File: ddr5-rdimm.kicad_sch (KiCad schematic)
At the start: 20 parts, among them J2 Bus_DDR5_DDR504111002KQ, Q10 BSS138PW, Q11 BSS138PW, Q9 BSS138PW, SW3 SW_KMR211NGLFS_SMD

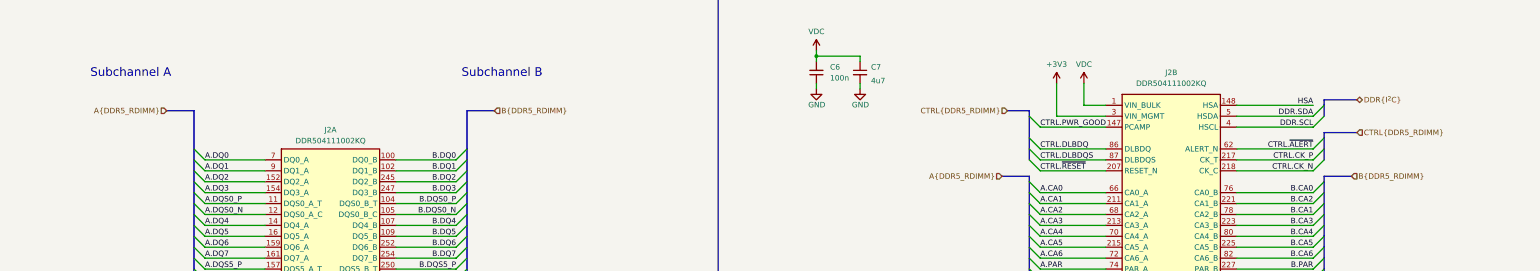
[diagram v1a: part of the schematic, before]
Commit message: [#68016] Improve bus entry marking
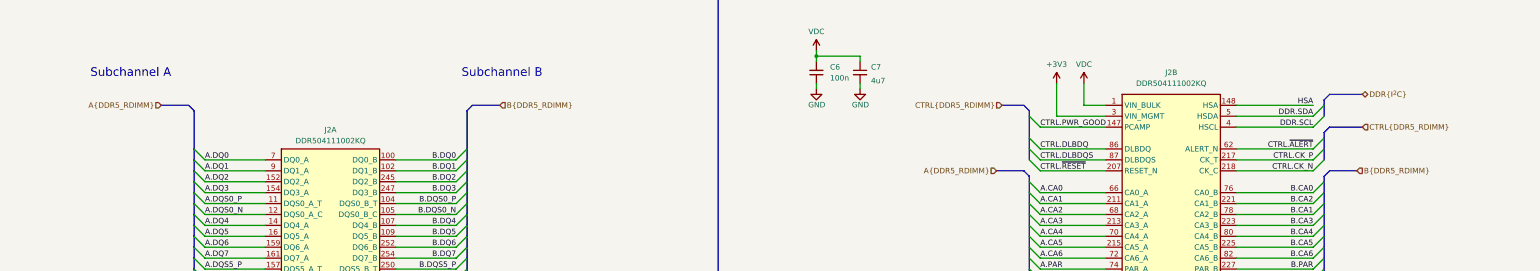
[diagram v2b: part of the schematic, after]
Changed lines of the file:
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@@
     (stroke (width 0) (type default))
   )
-  (bus (pts (xy 257.81 52.07) (xy 262.89 52.07))
+  (bus (pts (xy 256.54 50.8) (xy 261.62 50.8))
     (stroke (width 0) (type default))
   )
@@
     (stroke (width 0) (type default))
   )
+  (bus (pts (xy 262.89 67.31) (xy 261.62 66.04))
+    (stroke (width 0) (type default))
+  )
   (wire (pts (xy 71.12 76.2) (xy 85.09 76.2))
     (stroke (width 0) (type default))
@@
     (stroke (width 0) (type default))
   )
-  (bus (pts (xy 138.43 52.07) (xy 132.08 52.07))
+  (bus (pts (xy 139.7 50.8) (xy 133.35 50.8))
     (stroke (width 0) (type default))
   )
@@
     (stroke (width 0) (type default))
   )
+  (bus (pts (xy 332.74 66.04) (xy 331.47 67.31))
+    (stroke (width 0) (type default))
+  )
   (wire (pts (xy 115.57 114.3) (xy 129.54 114.3))
     (stroke (width 0) (type default))
@@
     (stroke (width 0) (type default))
   )
-  (bus (pts (xy 331.47 49.53) (xy 339.09 49.53))
+  (bus (pts (xy 332.74 48.26) (xy 340.36 48.26))
     (stroke (width 0) (type default))
   )
@@
     (stroke (width 0) (type default))
   )
+  (bus (pts (xy 67.31 50.8) (xy 68.58 52.07))
+    (stroke (width 0) (type default))
+  )
   (wire (pts (xy 71.12 147.32) (xy 85.09 147.32))
     (stroke (width 0) (type default))
@@
     (stroke (width 0) (type default))
   )
-  (bus (pts (xy 331.47 67.31) (xy 337.82 67.31))
+  (bus (pts (xy 332.74 66.04) (xy 339.09 66.04))
     (stroke (width 0) (type default))
   )
@@
     (stroke (width 0) (type default))
   )
-  (bus (pts (xy 331.47 57.15) (xy 339.09 57.15))
+  (bus (pts (xy 332.74 55.88) (xy 340.36 55.88))
     (stroke (width 0) (type default))
   )
@@
     (stroke (width 0) (type default))
   )
-  (bus (pts (xy 62.23 52.07) (xy 68.58 52.07))
+  (bus (pts (xy 60.96 50.8) (xy 67.31 50.8))
     (stroke (width 0) (type default))
   )
@@
     (stroke (width 0) (type default))
   )
+  (bus (pts (xy 262.89 52.07) (xy 261.62 50.8))
+    (stroke (width 0) (type default))
+  )
   (wire (pts (xy 313.69 114.3) (xy 313.69 111.76))
     (stroke (width 0) (type default))
@@
     (stroke (width 0) (type default))
   )
-  (bus (pts (xy 256.54 67.31) (xy 262.89 67.31))
+  (bus (pts (xy 255.27 66.04) (xy 261.62 66.04))
     (stroke (width 0) (type default))
   )
@@
     (stroke (width 0) (type default))
   )
+  (bus (pts (xy 132.08 52.07) (xy 133.35 50.8))
+    (stroke (width 0) (type default))
+  )
   (wire (pts (xy 115.57 152.4) (xy 129.54 152.4))
     (stroke (width 0) (type default))
@@
     (stroke (width 0) (type default))
   )
+  (bus (pts (xy 332.74 55.88) (xy 331.47 57.15))
+    (stroke (width 0) (type default))
+  )
   (wire (pts (xy 347.98 166.37) (xy 347.98 168.91))
     (stroke (width 0) (type default))
@@
     (stroke (width 0) (type default))
   )
+  (bus (pts (xy 332.74 48.26) (xy 331.47 49.53))
+    (stroke (width 0) (type default))
+  )
   (image (at 71.12 272.415) (scale 0.15)
     (data
@@
     )
   )
-  (hierarchical_label "DDR{I^{2}C}" (shape bidirectional) (at 339.09 49.53 0) (fields_autoplaced)
+  (hierarchical_label "DDR{I^{2}C}" (shape bidirectional) (at 340.36 48.26 0) (fields_autoplaced)
     (effects (font (size 1.27 1.27)) (justify left))
   )
-  (hierarchical_label "B{DDR5_RDIMM}" (shape input) (at 337.82 67.31 0) (fields_autoplaced)
+  (hierarchical_label "B{DDR5_RDIMM}" (shape input) (at 339.09 66.04 0) (fields_autoplaced)
     (effects (font (size 1.27 1.27)) (justify left))
   )
-  (hierarchical_label "A{DDR5_RDIMM}" (shape input) (at 62.23 52.07 180) (fields_autoplaced)
+  (hierarchical_label "A{DDR5_RDIMM}" (shape input) (at 60.96 50.8 180) (fields_autoplaced)
     (effects (font (size 1.27 1.27)) (justify right))
   )
-  (hierarchical_label "CTRL{DDR5_RDIMM}" (shape input) (at 257.81 52.07 180) (fields_autoplaced)
+  (hierarchical_label "CTRL{DDR5_RDIMM}" (shape input) (at 256.54 50.8 180) (fields_autoplaced)
     (effects (font (size 1.27 1.27)) (justify right))
   )
-  (hierarchical_label "CTRL{DDR5_RDIMM}" (shape input) (at 339.09 57.15 0) (fields_autoplaced)
+  (hierarchical_label "CTRL{DDR5_RDIMM}" (shape input) (at 340.36 55.88 0) (fields_autoplaced)
     (effects (font (size 1.27 1.27)) (justify left))
   )
-  (hierarchical_label "A{DDR5_RDIMM}" (shape input) (at 256.54 67.31 180) (fields_autoplaced)
+  (hierarchical_label "A{DDR5_RDIMM}" (shape input) (at 255.27 66.04 180) (fields_autoplaced)
     (effects (font (size 1.27 1.27)) (justify right))
   )
-  (hierarchical_label "B{DDR5_RDIMM}" (shape input) (at 138.43 52.07 0) (fields_autoplaced)
+  (hierarchical_label "B{DDR5_RDIMM}" (shape input) (at 139.7 50.8 0) (fields_autoplaced)
     (effects (font (size 1.27 1.27)) (justify left))
   )

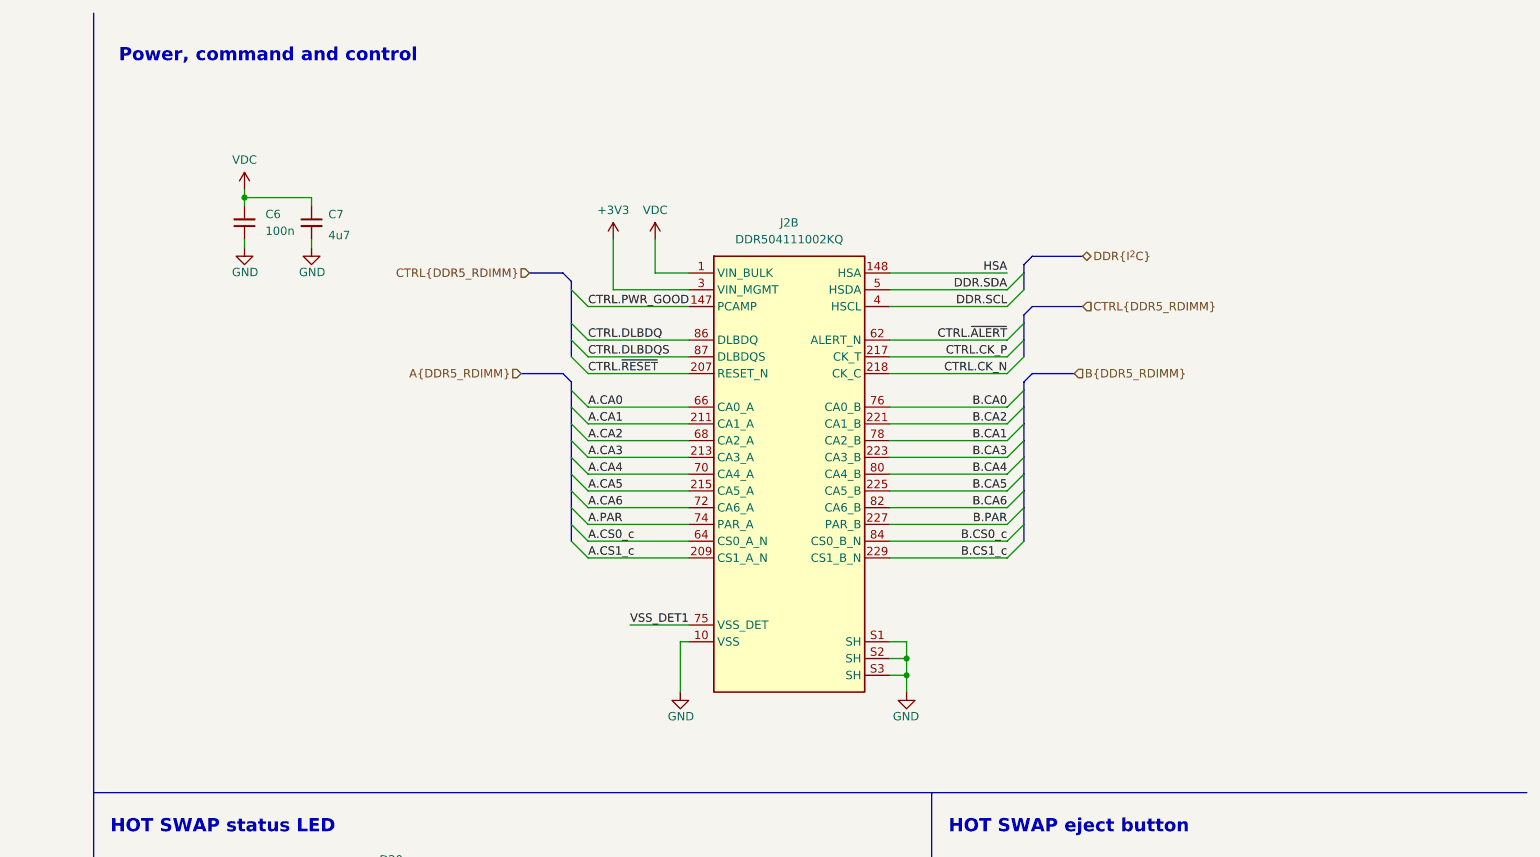
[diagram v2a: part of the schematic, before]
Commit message: [#67824] Finish length matching SPI flash interface. Add DDR5 power control transistors. Finish silkscreen labels replacement
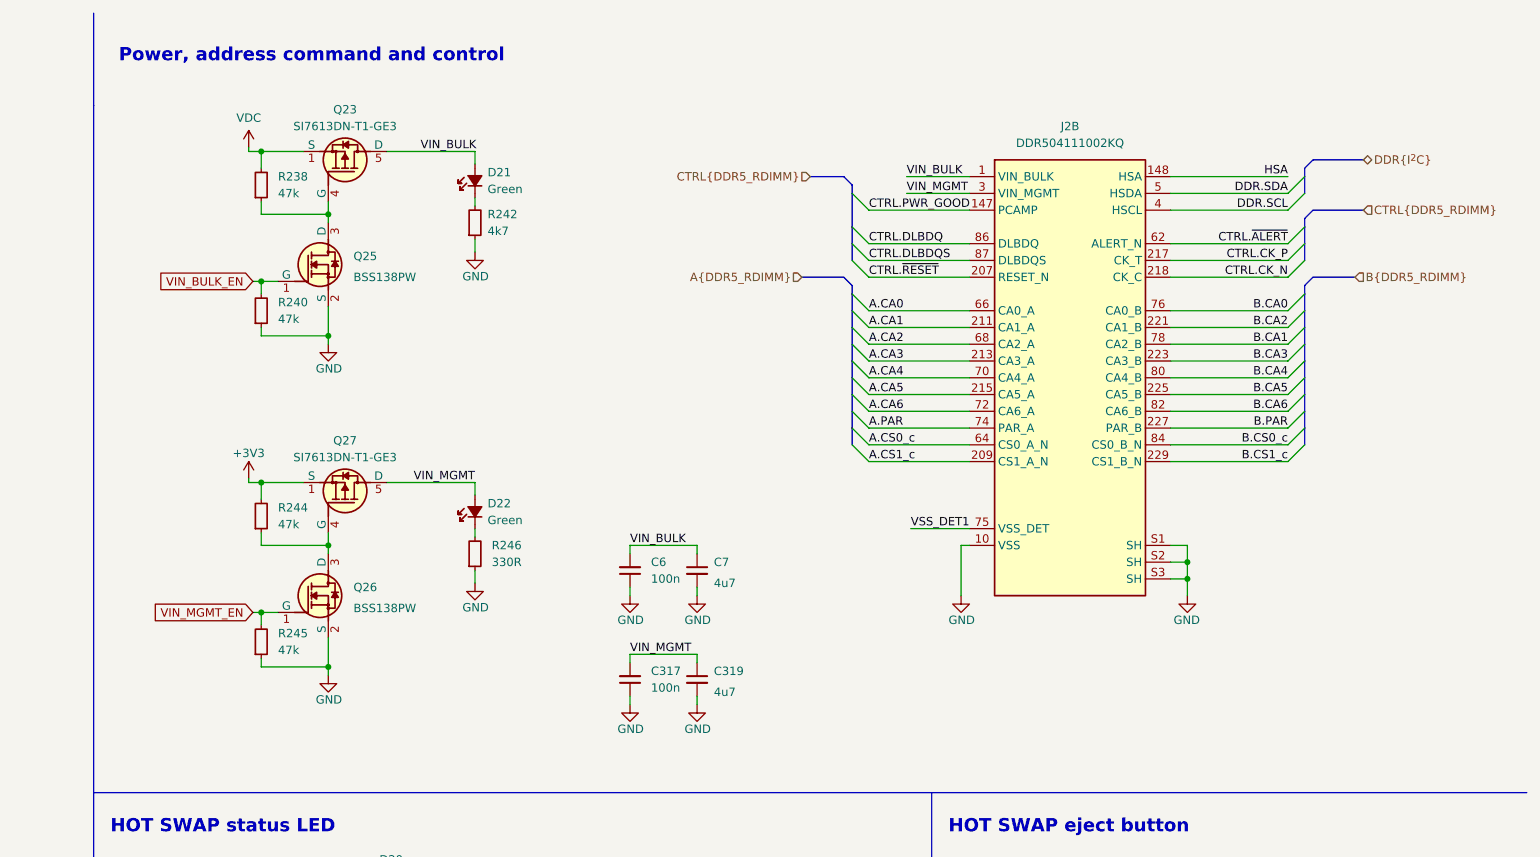
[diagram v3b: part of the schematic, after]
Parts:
- added C317: C_100n_0402, antmicro-footprints:C_0402_1005Metric, symbol antmicroCapacitors0402:C_100n_0402
- added C319: C_4u7_0402, antmicro-footprints:C_0402_1005Metric, symbol antmicroCapacitors0402:C_4u7_0402
- added D21, D22: LED_G_0402_VLMTG1500-GS08, antmicro-footprints:LED_0402_1005Metric_G, symbol antmicroLEDIndicationDiscrete:LED_G_0402_VLMTG1500-GS08
- added Q23, Q27: SI7613DN-T1-GE3, antmicro-footprints:Vishay_PowerPAK_1212-8_Single, symbol antmicroTransistorsFETsMOSFETsSingle:SI7613DN-T1-GE3
- added Q25, Q26: BSS138PW, antmicro-footprints:SC70-3, symbol antmicroTransistorsFETsMOSFETsSingle:BSS138PW
- added R238, R240, R244, R245: R_47k_0402, antmicro-footprints:R_0402_1005Metric, symbol antmicroResistors0402:R_47k_0402
- added R242: R_4k7_0402, antmicro-footprints:R_0402_1005Metric, symbol antmicroResistors0402:R_4k7_0402
- added R246: R_330R_0402, antmicro-footprints:R_0402_1005Metric, symbol antmicroResistors0402:R_330R_0402
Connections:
- net +3V3: now also Q27.1 (S), Q27.2 (S), Q27.3 (S), R244.2; no longer J2.3 (VIN_MGMT)
- net GND: now also C317.1, C319.2, Q25.2 (S), Q26.2 (S), R240.1, R242.1, R245.1, R246.1
- net VDC: now also Q23.1 (S), Q23.2 (S), Q23.3 (S), R238.2; no longer C6.2, C7.1, J2.1 (VIN_BULK), J2.145 (VIN_BULK), J2.146 (VIN_BULK)
- new net: Q26.3 (D), Q27.4 (G), R244.1
- new net: Q23.4 (G), Q25.3 (D), R238.1
- new net: D21.1 (C), R242.2
- new net: D22.1 (C), R246.2
- new net VIN_BULK: C6.2, C7.1, D21.2 (A), J2.1 (VIN_BULK), J2.145 (VIN_BULK), J2.146 (VIN_BULK), Q23.5 (D)
- new net VIN_BULK_EN: Q25.1 (G), R240.2
- new net VIN_MGMT: C317.2, C319.1, D22.2 (A), J2.3 (VIN_MGMT), Q27.5 (D)
- new net VIN_MGMT_EN: Q26.1 (G), R245.2
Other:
- note added: "Power, address command and control"
- note removed: "Power, command and control"
- moved on the sheet: C6, C7, J2B

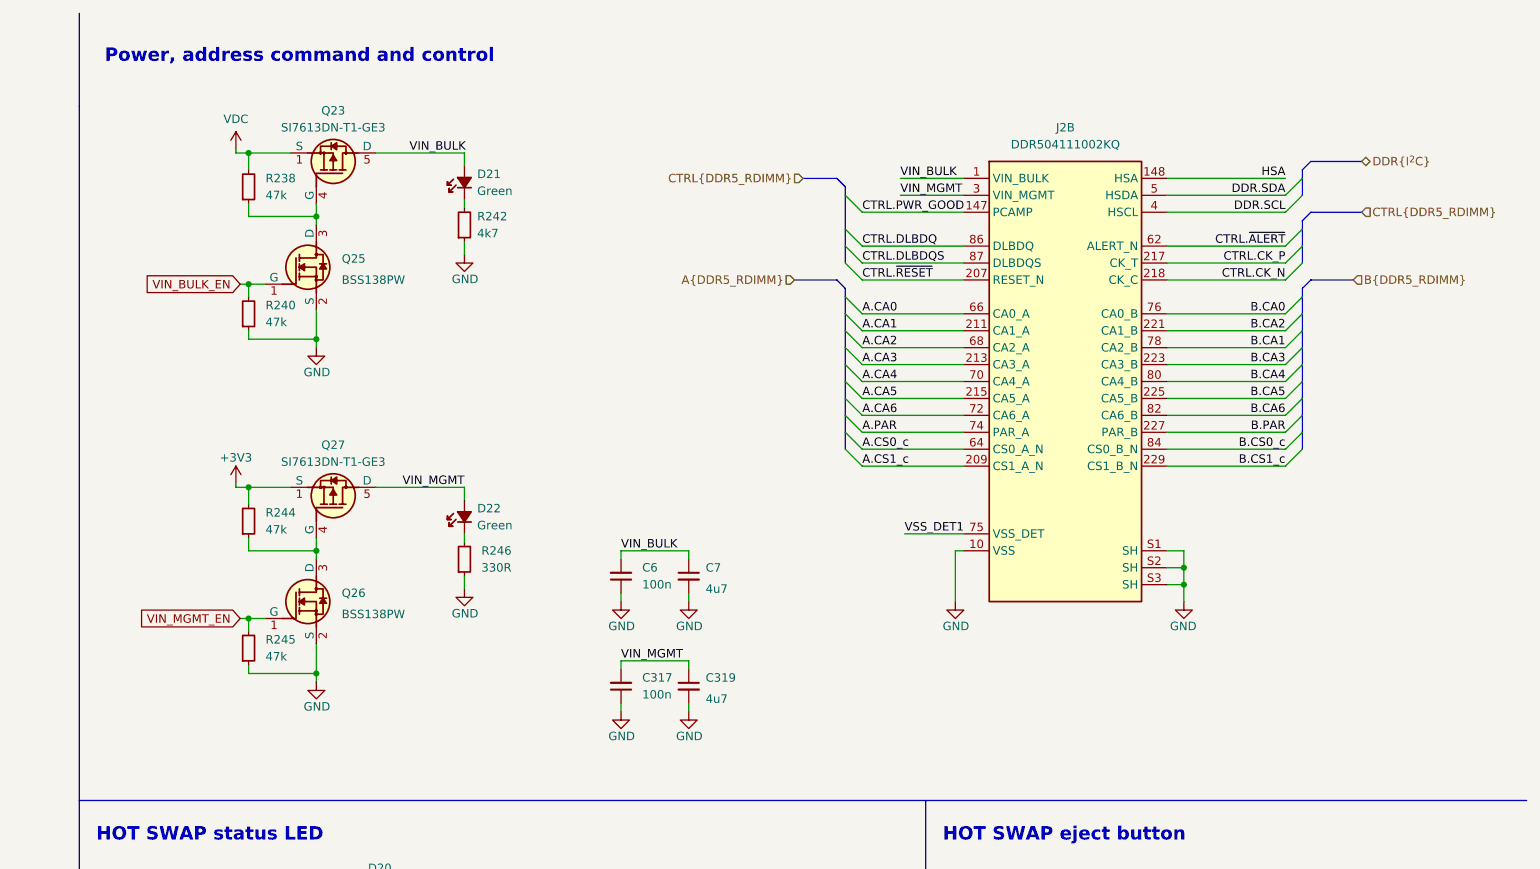
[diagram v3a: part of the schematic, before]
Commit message: [#68016] Solve ERC warrings and errors
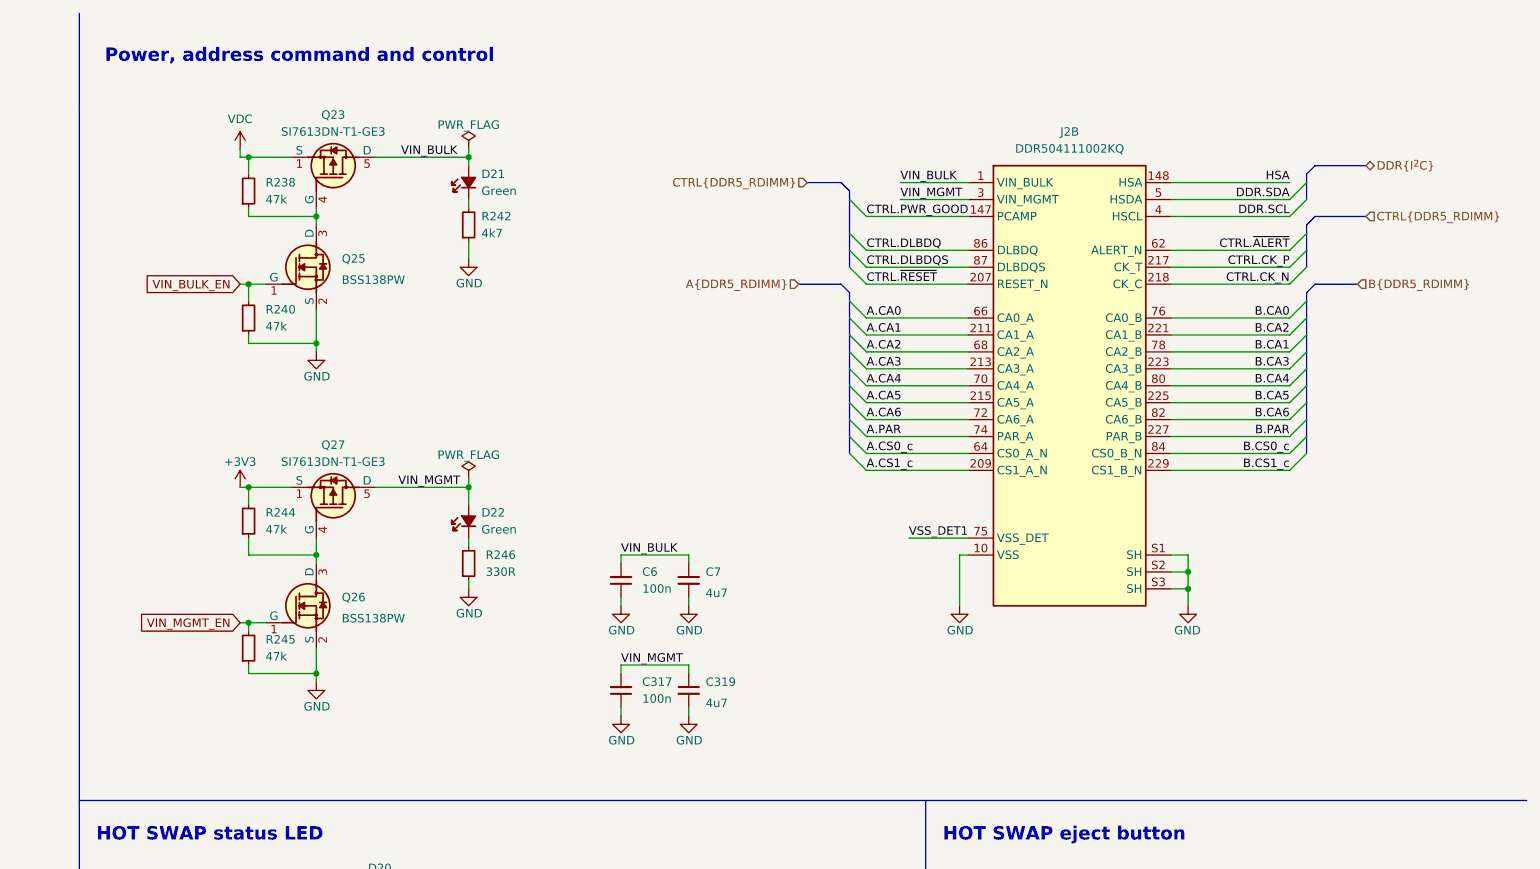
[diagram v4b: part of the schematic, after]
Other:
- moved on the sheet: C317, C319, C6, C7, D21, D22, J2B, Q23, Q26, R238, R240, R242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
